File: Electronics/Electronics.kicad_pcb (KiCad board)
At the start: 2 copper layers, 4 parts, among them U1 DRV8871DDA, U2 MT3608, U3 MAX98357A, U4 IP2721

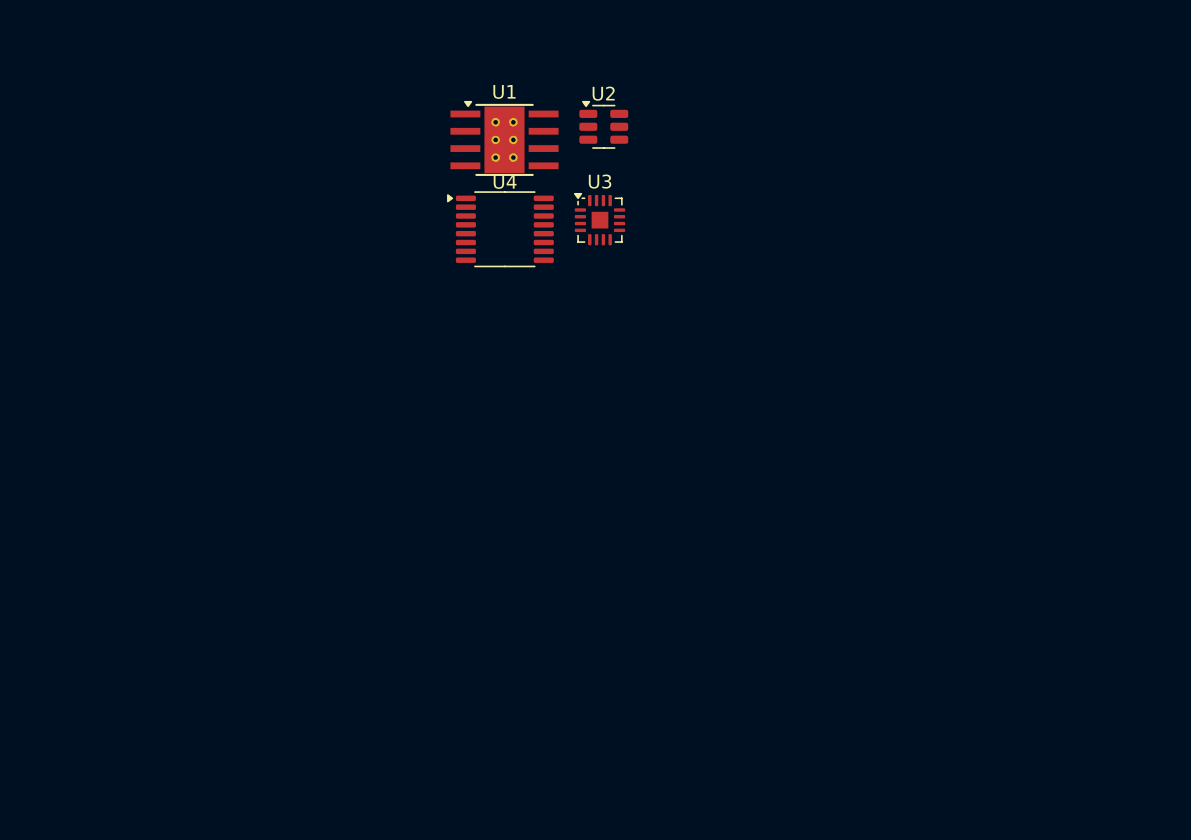
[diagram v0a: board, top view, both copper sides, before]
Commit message: V1 schematic and PCB are laid out and ready for production
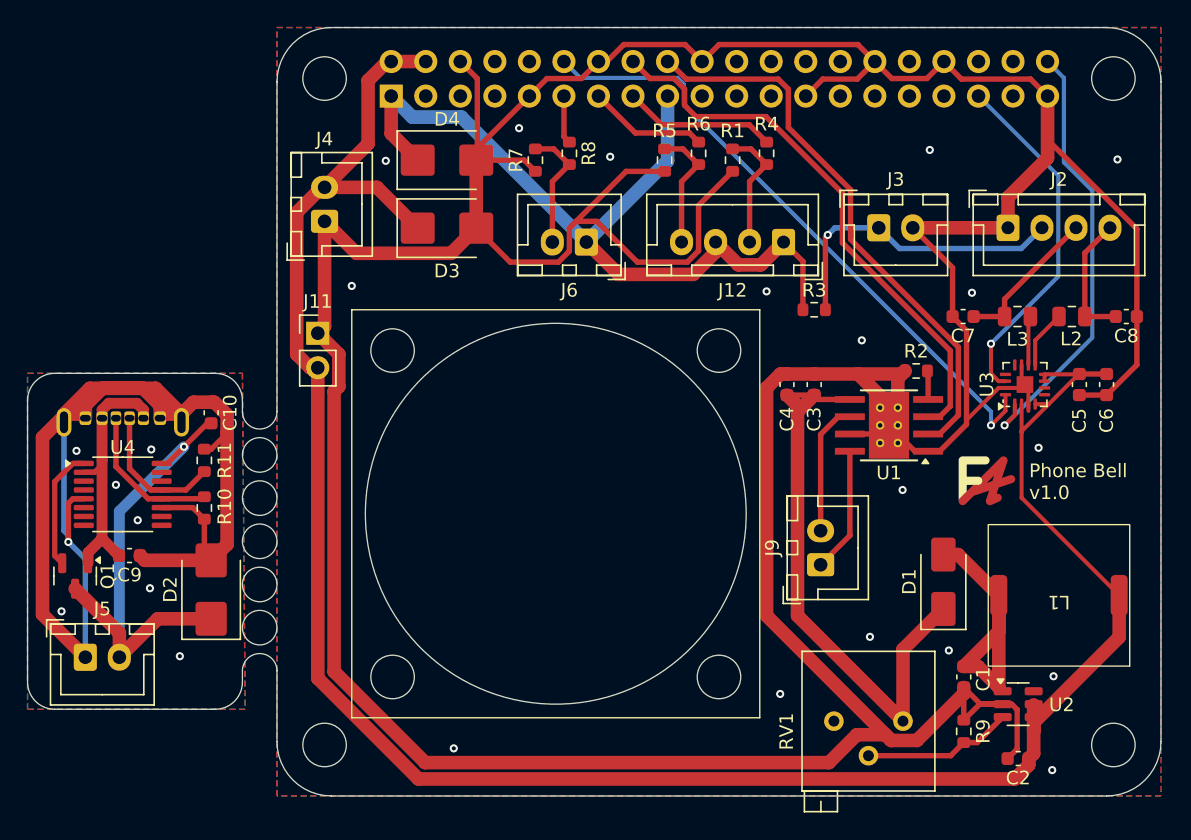
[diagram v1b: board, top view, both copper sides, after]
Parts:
- added C1: 10uF, Capacitor_SMD:C_0603_1608Metric, F.Cu at (162.0, 119.2)
- added C10: 10uF, Capacitor_SMD:C_0603_1608Metric, F.Cu at (106.7, 99.7)
- added C2: 20uF, Capacitor_SMD:C_0603_1608Metric, F.Cu at (166.0, 125.2)
- added C3: 0.1uF, Capacitor_SMD:C_0603_1608Metric, F.Cu at (151.0, 97.7)
- added C4: 22uF, Capacitor_SMD:C_0603_1608Metric, F.Cu at (149.0, 97.7)
- added C5: 0.1uF, Capacitor_SMD:C_0603_1608Metric, F.Cu at (170.5, 97.7)
- added C6: 10uF, Capacitor_SMD:C_0603_1608Metric, F.Cu at (172.5, 97.7)
- added C7: 220pf, Capacitor_SMD:C_0603_1608Metric, F.Cu at (161.9, 92.7)
- added C8: 220pf, Capacitor_SMD:C_0603_1608Metric, F.Cu at (173.9, 92.7)
- added C9: 1uF, Capacitor_SMD:C_0603_1608Metric, F.Cu at (100.7, 110.2)
- added D1: SS34, Diode_SMD:D_SMA, F.Cu at (160.5, 112.2)
- added D2: SMBJ6.0CA, Diode_SMD:D_SMB, F.Cu at (106.7, 112.7)
- added D3: SMBJ6.0CA, Diode_SMD:D_SMB, F.Cu at (124.0, 86.2)
- added D4: SMBJ6.0CA, Diode_SMD:D_SMB, F.Cu at (124.0, 81.2)
- added J1: Raspberry_Pi_2_3, Connector_PinSocket_2.54mm:PinSocket_2x20_P2.54mm_Vertical, B.Cu at (119.9, 76.4)
- added J10: USB_C_Receptacle_PowerOnly_6P, AdditionalComponents:YIYUAN YTC-TC6-465, B.Cu at (100.2, 100.4)
- added J11: FAN_OUT, Connector_PinHeader_2.54mm:PinHeader_1x02_P2.54mm_Vertical, F.Cu at (114.5, 93.9)
- added J12: DIAL, Connector_JST:JST_XH_B4B-XH-A_1x04_P2.50mm_Vertical, F.Cu at (148.8, 87.2)
- added J2: HANDSET, Connector_JST:JST_XH_B4B-XH-A_1x04_P2.50mm_Vertical, F.Cu at (165.2, 86.1)
- added J3: EXT_ADC, Connector_JST:JST_XH_B2B-XH-A_1x02_P2.50mm_Vertical, F.Cu at (155.8, 86.1)
- added J4: USB-C_PD_IN, Connector_JST:JST_XH_B2B-XH-A_1x02_P2.50mm_Vertical, F.Cu at (115.0, 85.7)
- added J5: USB-C_PD_OUT, Connector_JST:JST_XH_B2B-XH-A_1x02_P2.50mm_Vertical, F.Cu at (97.4, 117.7)
- added J6: HOOK_SWITCH_TERM, Connector_JST:JST_XH_B2B-XH-A_1x02_P2.50mm_Vertical, F.Cu at (134.2, 87.2)
- added J9: RINGER_BELL, Connector_JST:JST_XH_B2B-XH-A_1x02_P2.50mm_Vertical, F.Cu at (151.5, 110.9)
- added L1: 22uH, AdditionalComponents:CYL104R-22UH, F.Cu at (169.0, 113.2)
- added L2: 445-1555-2-ND, Capacitor_SMD:C_0805_2012Metric, F.Cu at (169.9, 92.7)
- added L3: 445-1555-2-ND, Capacitor_SMD:C_0805_2012Metric, F.Cu at (165.9, 92.7)
- added Q1: AO3400A, Package_TO_SOT_SMD:SOT-23, F.Cu at (96.7, 111.7)
- added R1: 10K, Resistor_SMD:R_0603_1608Metric, F.Cu at (145.0, 81.2)
- added R10: 5.1K, Resistor_SMD:R_0603_1608Metric, F.Cu at (106.2, 106.7)
- added R11: 5.1K, Resistor_SMD:R_0603_1608Metric, F.Cu at (106.2, 103.2)
- added R2: 30K, Resistor_SMD:R_0603_1608Metric, F.Cu at (158.5, 96.7)
- added R3: 1K, Resistor_SMD:R_0603_1608Metric, F.Cu at (151.0, 92.2)
- added R4: 220, Resistor_SMD:R_0603_1608Metric, F.Cu at (147.5, 80.7)
- added R5: 10K, Resistor_SMD:R_0603_1608Metric, F.Cu at (140.0, 81.2)
- added R6: 220, Resistor_SMD:R_0603_1608Metric, F.Cu at (142.5, 80.7)
- added R7: 10K, Resistor_SMD:R_0603_1608Metric, F.Cu at (130.5, 81.2)
- added R8: 220, Resistor_SMD:R_0603_1608Metric, F.Cu at (133.0, 80.7)
- added R9: 2.2k, Resistor_SMD:R_0603_1608Metric, F.Cu at (162.0, 123.2)
- added REF**: MountingHole_3.2mm_M3, MountingHole:MountingHole_3.2mm_M3, F.Cu at (115.0, 75.2)
- added REF**: MountingHole_3.2mm_M3, MountingHole:MountingHole_3.2mm_M3, F.Cu at (173.0, 124.2)
- added REF**: Logo, AdditionalComponents:Logo, F.Cu at (163.6, 102.9)
- added REF**: MountingHole_3.2mm_M3, MountingHole:MountingHole_3.2mm_M3, F.Cu at (144.0, 95.2)
- added REF**: MountingHole_3.2mm_M3, MountingHole:MountingHole_3.2mm_M3, F.Cu at (120.0, 119.2)
- added REF**: MountingHole_3.2mm_M3, MountingHole:MountingHole_3.2mm_M3, F.Cu at (115.0, 124.2)
- added REF**: MountingHole_3.2mm_M3, MountingHole:MountingHole_3.2mm_M3, F.Cu at (173.0, 75.2)
- added REF**: MountingHole_3.2mm_M3, MountingHole:MountingHole_3.2mm_M3, F.Cu at (144.0, 119.2)
- added REF**: MountingHole_3.2mm_M3, MountingHole:MountingHole_3.2mm_M3, F.Cu at (120.0, 95.2)
- added RV1: 3296P-1-104, Potentiometer_THT:Potentiometer_Bourns_3296P_Horizontal, F.Cu at (152.4, 122.4)
- moved U2 52.3 mm to (166.0, 121.2)
- moved U1 35.2 mm to (156.5, 100.7), turned to 180 degrees
- moved U4 34.2 mm to (100.2, 105.7)
- moved U3 33.5 mm to (166.5, 97.7), turned to 90 degrees
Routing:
- net GND: track 0.00 -> 352.7 mm, vias 0 -> 17
- net +5V: track 0.00 -> 163.2 mm
- net USB-C_PD_GND: track 0.00 -> 93.8 mm, vias 0 -> 8
- net +3.3V: track 0.00 -> 61.4 mm
- net HANDSET_DAC_BCLK: track 0.00 -> 46.6 mm, vias 0 -> 1
- net +24V: track 0.00 -> 43.5 mm
- net RINGER_BELL_IN2: track 0.00 -> 41.7 mm
- net RINGER_BELL_IN1: track 0.00 -> 41.0 mm
- net USB-C_PD_+5V: track 0.00 -> 36.6 mm, vias 0 -> 1
- net HANDSET_DAC_DIN: track 0.00 -> 32.7 mm, vias 0 -> 1
- net HANDSET_DAC_LRCLK: track 0.00 -> 26.2 mm, vias 0 -> 1
- net Net-(J2-Pin_2): track 0.00 -> 22.8 mm, vias 0 -> 1
- net Net-(D1-A): track 0.00 -> 22.0 mm
- net Net-(Q1-D): track 0.00 -> 19.8 mm
- net DIAL_PULSE: track 0.00 -> 11.2 mm
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- added copper zone on B.Cu, net GND
- added copper zone on F.Cu, net GND
- added copper zone on B.Cu, net USB-C_PD_GND
- added copper zone on F.Cu, net USB-C_PD_GND
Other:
- board outline added: 83.3 x 56.5 mm
- board text added: "Phone Bell v1.0"

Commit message: Finalized production exports and now awaiting PCBs to arrive
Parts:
- L1: value 22uH -> YPRH104R-220M; footprint AdditionalComponents:CYL104R-22UH -> AdditionalComponents:YPRH104R-220M
- moved C3 2.68 mm to (153.0, 95.8)
- moved C4 1.09 mm to (149.9, 98.3)
- moved C1 0.53 mm to (162.0, 118.6)
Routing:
- net +24V: track 43.5 -> 46.5 mm
- net GND: track 352.7 -> 353.6 mm
- net Net-(D1-A): track 22.0 -> 21.4 mm

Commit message: Updated USB-C port on PCB, made test emulator for validating functionality.
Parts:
- J10: footprint AdditionalComponents:YIYUAN YTC-TC6-465 -> AdditionalComponents:YIYUAN YTC-TC6-560
- moved J10 0.80 mm to (100.2, 99.6)
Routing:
- net USB-C_PD_GND: track 93.8 -> 84.3 mm
- net Net-(Q1-D): track 19.8 -> 21.5 mm, vias 0 -> 1
- net Net-(J10-CC2): track 11.0 -> 10.7 mm, vias 0 -> 1
- net Net-(J10-CC1): track 10.3 -> 10.0 mm, vias 0 -> 1
